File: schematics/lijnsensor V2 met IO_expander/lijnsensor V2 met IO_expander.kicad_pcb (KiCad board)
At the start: 2 copper layers, 137 x 105 mm, 32 parts, among them J2 Conn_01x05_Pin, U1 USBLC6-2SC6, U10 AS7343xDLG, U11 AS7343xDLG, U12 TCA9535RGER, U2 TCA9548ARGER, U3 TLV75718PDBV, U4 AS7343xDLG, U5 AS7343xDLG, U6 AS7343xDLG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

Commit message: begin al met het toevoegen van de io extender nog niet klaar
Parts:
- added H1: MountingHole, MountingHole:MountingHole_4.3mm_M4, F.Cu at (145.0, 70.5)
- added H2: MountingHole, MountingHole:MountingHole_4.3mm_M4, F.Cu at (145.0, 56.5)
- added H3: MountingHole, MountingHole:MountingHole_4.3mm_M4, F.Cu at (90.5, 56.5)
- added H4: MountingHole, MountingHole:MountingHole_4.3mm_M4, F.Cu at (90.5, 70.5)
- added H5: MountingHole, MountingHole:MountingHole_8.4mm_M8, F.Cu at (56.0, 150.0)
- added H6: MountingHole, MountingHole:MountingHole_8.4mm_M8, F.Cu at (181.0, 150.0)
- U12: footprint Package_DFN_QFN:VQFN-24-1EP_4x4mm_P0.5mm_EP2.45x2.45mm -> Package_DFN_QFN:Texas_RGE0024H_VQFN-24-1EP_4x4mm_P0.5mm_EP2.7x2.7mm
- U2: footprint Package_DFN_QFN:Texas_RGE0024C_VQFN-24-1EP_4x4mm_P0.5mm_EP2.1x2.1mm -> Package_DFN_QFN:Texas_RGE0024H_VQFN-24-1EP_4x4mm_P0.5mm_EP2.7x2.7mm
- moved R10 93.5 mm to (133.7, 57.6)
- moved R3 93.5 mm to (181.2, 137.2)
- moved R9 93.5 mm to (136.2, 55.1)
- moved U4 93.5 mm to (181.0, 140.0)
- moved U7 93.5 mm to (136.0, 58.0)
- moved R4 93.5 mm to (178.7, 139.6)
- moved R5 31.8 mm to (181.1, 105.2)
- moved R7 31.8 mm to (161.6, 80.1)
- moved R6 31.0 mm to (178.9, 107.6)
- moved R8 31.0 mm to (160.8, 82.3)
- moved U5 30.8 mm to (181.0, 108.0)
- moved U6 30.8 mm to (163.0, 83.0)
- moved U12 19.9 mm to (123.0, 59.5), turned to 180 degrees
- moved U2 19.4 mm to (113.0, 59.5), turned to 180 degrees
- moved R17 9.21 mm to (113.9, 62.9), turned to 0 degrees
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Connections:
- R10 pad 2: Net-(U2-SC0) -> Net-(U2-SC3)
- R3 pad 2: Net-(U2-SD3) -> Net-(U2-SD0)
- R4 pad 2: Net-(U2-SC3) -> Net-(U2-SC0)
- R5 pad 2: Net-(U2-SD2) -> Net-(U2-SD1)
- R6 pad 2: Net-(U2-SC2) -> Net-(U2-SC1)
- R7 pad 2: Net-(U2-SD1) -> Net-(U2-SC2)
- R8 pad 2: Net-(U2-SC1) -> Net-(U2-SD2)
- R9 pad 2: Net-(U2-SD0) -> Net-(U2-SD3)
- U10 pad 6: unconnected-(U10-GPIO-Pad6) -> Net-(U10-GPIO)
- U10 pad 7: unconnected-(U10-INT-Pad7) -> Net-(U10-INT)
- U11 pad 6: unconnected-(U11-GPIO-Pad6) -> Net-(U11-GPIO)
- U11 pad 7: unconnected-(U11-INT-Pad7) -> Net-(U11-INT)
- U12 pad 1: unconnected-(U12-P00-Pad1) -> Net-(U12-P00)
- U12 pad 10: unconnected-(U12-P10-Pad10) -> Net-(U12-P10)
- U12 pad 11: unconnected-(U12-P11-Pad11) -> Net-(U12-P11)
- U12 pad 12: unconnected-(U12-P12-Pad12) -> Net-(U12-P12)
- U12 pad 13: unconnected-(U12-P13-Pad13) -> Net-(U12-P13)
- U12 pad 14: unconnected-(U12-P14-Pad14) -> Net-(U12-P14)
- U12 pad 15: unconnected-(U12-P15-Pad15) -> Net-(U12-P15)
- U12 pad 16: unconnected-(U12-P16-Pad16) -> Net-(U10-INT)
- U12 pad 17: unconnected-(U12-P17-Pad17) -> Net-(U11-INT)
- U12 pad 2: unconnected-(U12-P01-Pad2) -> Net-(U12-P01)
- U12 pad 3: unconnected-(U12-P02-Pad3) -> Net-(U12-P02)
- U12 pad 4: unconnected-(U12-P03-Pad4) -> Net-(U12-P03)
- U12 pad 5: unconnected-(U12-P04-Pad5) -> Net-(U12-P04)
- U12 pad 6: unconnected-(U12-P05-Pad6) -> Net-(U12-P05)
- U12 pad 7: unconnected-(U12-P06-Pad7) -> Net-(U10-GPIO)
- U12 pad 8: unconnected-(U12-P07-Pad8) -> Net-(U11-GPIO)
- U2 pad 25: unconnected-(U2-1EP-Pad25) -> GND
- U4 pad 2: Net-(U2-SC3) -> Net-(U2-SC0)
- U4 pad 6: unconnected-(U4-GPIO-Pad6) -> Net-(U12-P00)
- U4 pad 7: unconnected-(U4-INT-Pad7) -> Net-(U12-P10)
- U4 pad 8: Net-(U2-SD3) -> Net-(U2-SD0)
- U5 pad 2: Net-(U2-SC2) -> Net-(U2-SC1)
- U5 pad 6: unconnected-(U5-GPIO-Pad6) -> Net-(U12-P01)
- U5 pad 7: unconnected-(U5-INT-Pad7) -> Net-(U12-P11)
- U5 pad 8: Net-(U2-SD2) -> Net-(U2-SD1)
- U6 pad 2: Net-(U2-SC1) -> Net-(U2-SD2)
- U6 pad 6: unconnected-(U6-GPIO-Pad6) -> Net-(U12-P02)
- U6 pad 7: unconnected-(U6-INT-Pad7) -> Net-(U12-P12)
- U6 pad 8: Net-(U2-SD1) -> Net-(U2-SC2)
- U7 pad 2: Net-(U2-SC0) -> Net-(U2-SC3)
- U7 pad 6: unconnected-(U7-GPIO-Pad6) -> Net-(U12-P03)
- U7 pad 7: unconnected-(U7-INT-Pad7) -> Net-(U12-P13)
- U7 pad 8: Net-(U2-SD0) -> Net-(U2-SD3)
- U8 pad 6: unconnected-(U8-GPIO-Pad6) -> Net-(U12-P04)
- U8 pad 7: unconnected-(U8-INT-Pad7) -> Net-(U12-P14)
- U9 pad 6: unconnected-(U9-GPIO-Pad6) -> Net-(U12-P05)
- U9 pad 7: unconnected-(U9-INT-Pad7) -> Net-(U12-P15)
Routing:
- net Net-(U2-SC0): track 118.9 -> 1.98 mm
- net Net-(U2-SD0): track 117.4 -> 2.95 mm, vias 2 -> 1
- net Net-(U2-SD1): track 87.1 -> 1.73 mm, vias 2 -> 0
- net Net-(U2-SC1): track 87.0 -> 1.86 mm, vias 2 -> 0
- net Net-(U11-GPIO): track 0.00 -> 83.1 mm
- net Net-(U11-INT): track 0.00 -> 83.0 mm
- net Net-(U10-GPIO): track 0.00 -> 62.3 mm
- net Net-(U10-INT): track 0.00 -> 55.5 mm
- net Net-(U2-SC2): track 57.9 -> 3.68 mm, vias 2 -> 1
- net Net-(U2-SD2): track 54.9 -> 6.13 mm
- net Net-(U12-P15): track 0.00 -> 33.2 mm, vias 0 -> 1
- net Net-(U12-P05): track 0.00 -> 29.6 mm, vias 0 -> 1
- net Net-(U2-SD3): track 18.7 -> 1.89 mm, vias 2 -> 0
- net Net-(U2-SC3): track 15.7 -> 2.09 mm
- net +3.3V: track 11.3 -> 24.7 mm, vias 3 -> 6
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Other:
- outline, holes or cut-outs redrawn

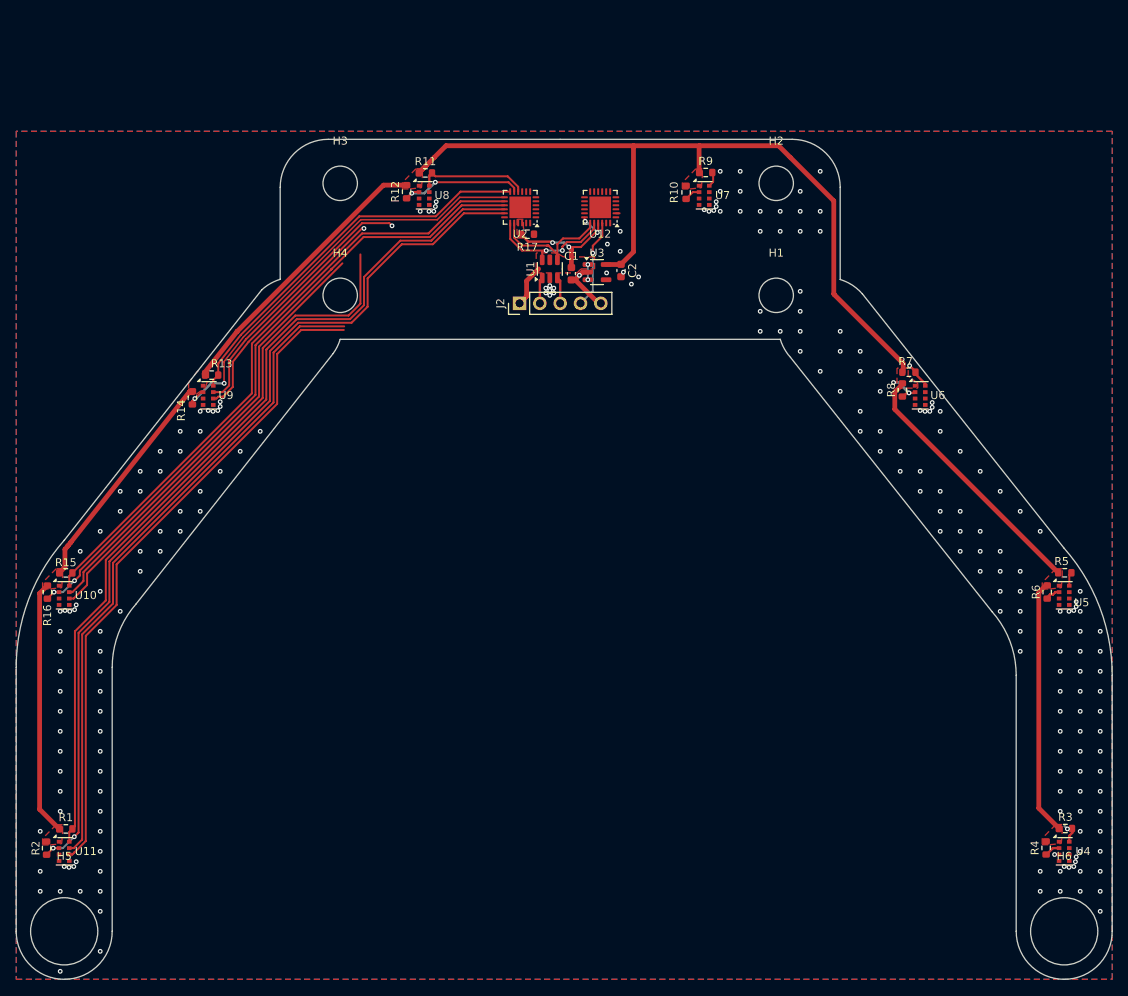
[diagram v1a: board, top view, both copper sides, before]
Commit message: de linker kant is al klaar nu nog de rechter kant van lijnsensor V2 met IO_expander
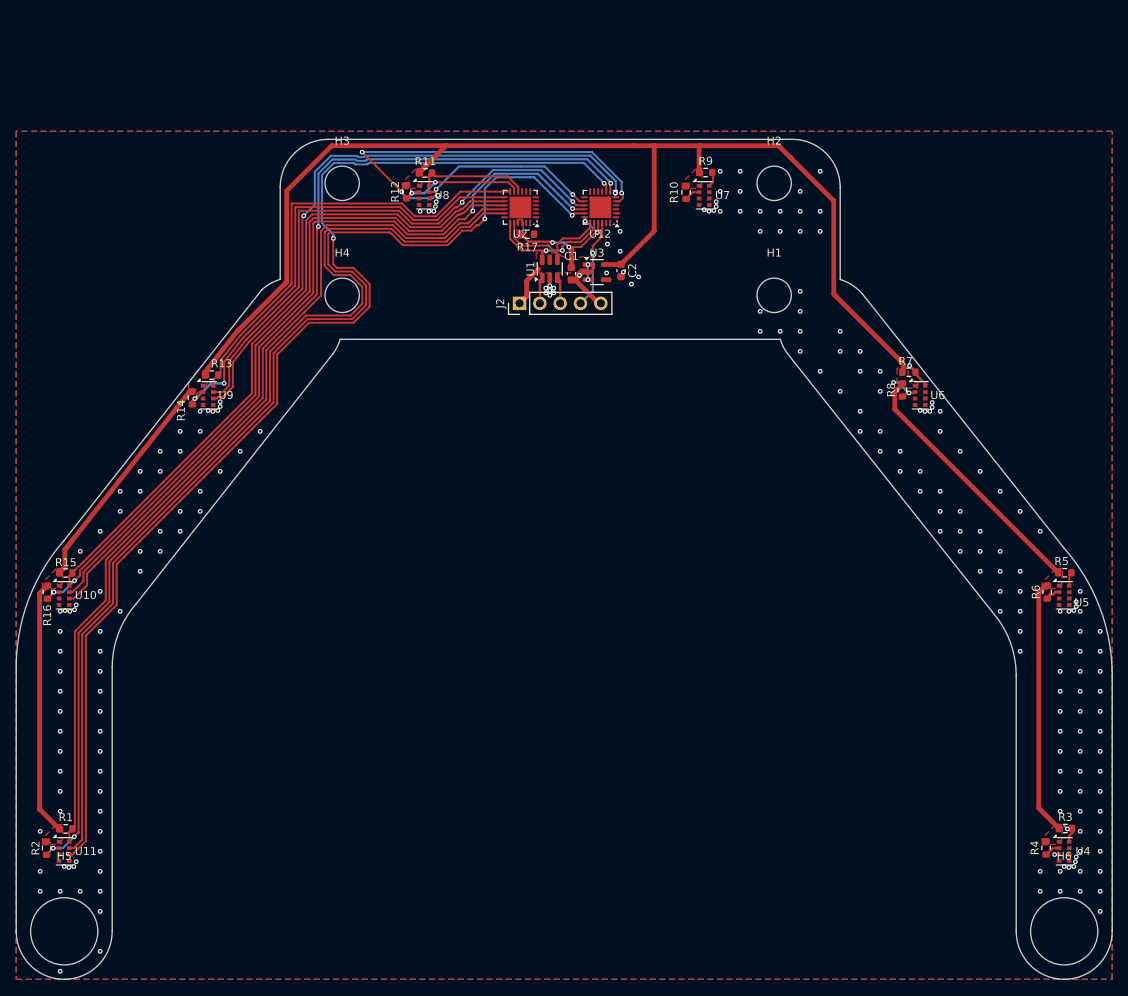
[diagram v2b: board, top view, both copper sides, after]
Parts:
- moved H1 0.25 mm to (144.8, 70.5)
- moved H2 0.25 mm to (144.8, 56.5)
- moved H3 0.25 mm to (90.8, 56.5)
- moved H4 0.25 mm to (90.8, 70.5)
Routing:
- net Net-(U11-GPIO): track 83.1 -> 145.9 mm, vias 0 -> 2
- net Net-(U11-INT): track 83.0 -> 139.5 mm, vias 0 -> 2
- net Net-(U12-P04): track 0.00 -> 50.6 mm, vias 0 -> 4
- net Net-(U12-P05): track 29.6 -> 76.0 mm, vias 1 -> 2
- net Net-(U10-INT): track 55.5 -> 99.7 mm, vias 0 -> 2
- net Net-(U10-GPIO): track 62.3 -> 106.1 mm, vias 0 -> 2
- net Net-(U12-P15): track 33.2 -> 68.7 mm, vias 1 -> 2
- net Net-(U12-P14): track 0.00 -> 22.5 mm, vias 0 -> 2
- net +1V8: track 263.1 -> 277.8 mm
- net Net-(U11-SCL): track 114.5 -> 126.8 mm
- net Net-(U2-SC5): track 53.3 -> 63.0 mm
- net Net-(U2-SD5): track 48.7 -> 55.9 mm
- net Net-(U10-SDA): track 78.7 -> 85.0 mm
- net Net-(U10-SCL): track 82.3 -> 88.5 mm
- net Net-(U11-SDA): track 111.1 -> 115.0 mm

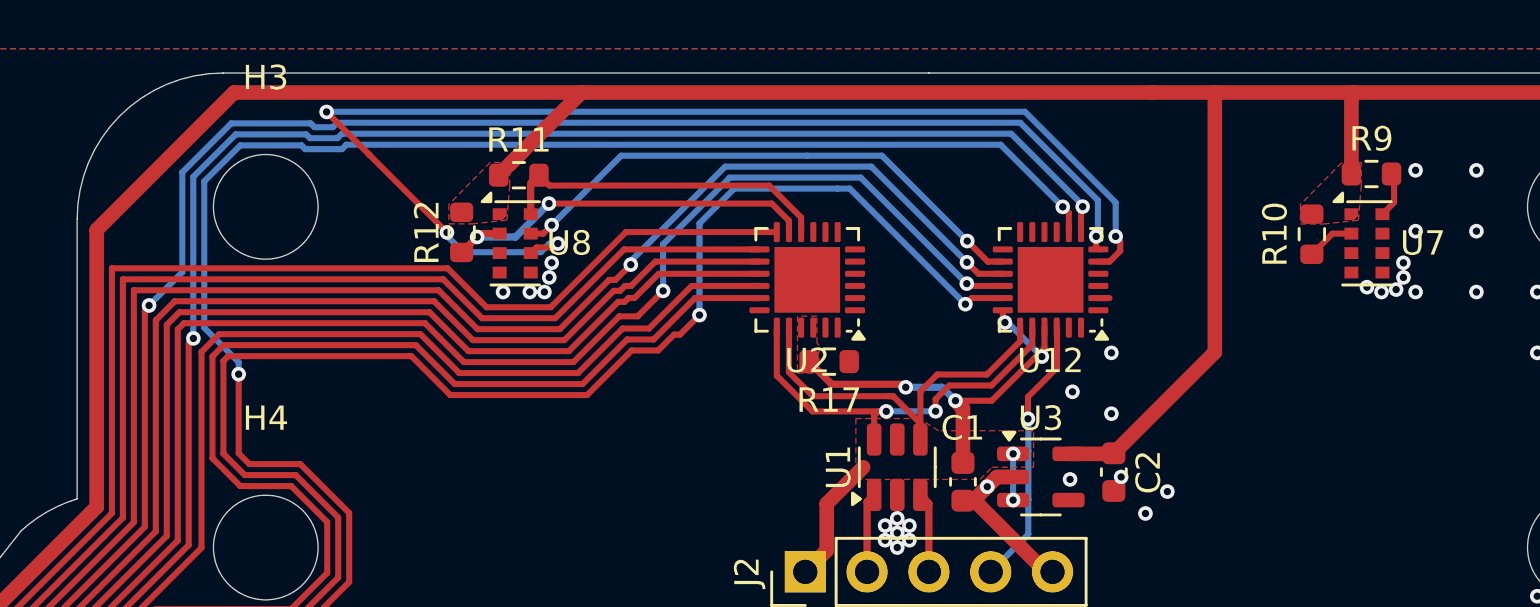
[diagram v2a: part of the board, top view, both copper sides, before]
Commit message: al begonnen aan de rechterkand van lijnsensor V2 met IO_expander
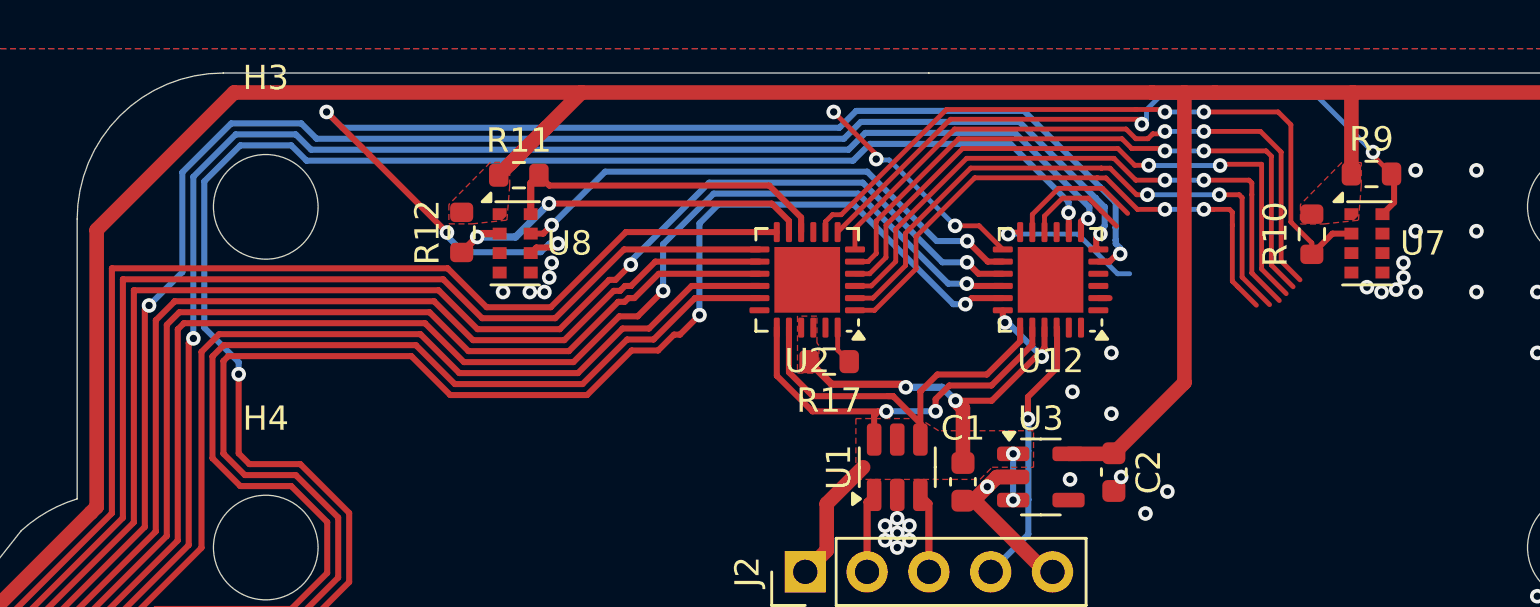
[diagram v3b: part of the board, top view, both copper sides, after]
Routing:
- net Net-(U2-SC3): track 2.09 -> 29.5 mm, vias 0 -> 2
- net Net-(U2-SD3): track 1.89 -> 28.8 mm, vias 0 -> 2
- net Net-(U2-SC2): track 3.68 -> 30.0 mm, vias 1 -> 3
- net Net-(U2-SD2): track 6.13 -> 32.1 mm, vias 2 -> 4
- net Net-(U2-SC1): track 1.86 -> 27.5 mm, vias 0 -> 2
- net Net-(U2-SD1): track 1.73 -> 26.7 mm, vias 0 -> 2
- net Net-(U2-SC0): track 1.98 -> 26.2 mm, vias 0 -> 2
- net Net-(U2-SD0): track 2.95 -> 26.3 mm, vias 1 -> 3
- net Net-(U12-P13): track 0.00 -> 9.40 mm, vias 0 -> 3
- net Net-(U12-P12): track 0.00 -> 6.20 mm, vias 0 -> 1
- net Net-(U12-P11): track 0.00 -> 5.51 mm
- net Net-(U12-P10): track 0.00 -> 4.40 mm
- net Net-(U2-~{RESET}): track 0.00 -> 1.59 mm
- net Net-(U10-GPIO): track 106.1 -> 107.4 mm
- net Net-(U11-GPIO): track 145.9 -> 146.6 mm
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
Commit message: klaar met het tekenen van alle verbindingen en veel via's geplaatst
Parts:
- moved R7 0.29 mm to (161.3, 80.1)
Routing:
- net Net-(U12-P10): track 4.40 -> 120.4 mm, vias 0 -> 4
- net Net-(U12-P00): track 0.00 -> 113.1 mm, vias 0 -> 4
- net Net-(U2-SC0): track 26.2 -> 131.3 mm
- net Net-(U2-SD0): track 26.3 -> 130.5 mm, vias 3 -> 4
- net Net-(U12-P11): track 5.51 -> 92.4 mm, vias 0 -> 4
- net Net-(U12-P01): track 0.46 -> 84.1 mm, vias 0 -> 4
- net Net-(U2-SD1): track 26.7 -> 103.2 mm, vias 2 -> 4
- net Net-(U2-SC1): track 27.5 -> 100.6 mm, vias 2 -> 4
- net Net-(U12-P02): track 0.00 -> 53.4 mm, vias 0 -> 4
- net Net-(U12-P12): track 6.20 -> 56.2 mm, vias 1 -> 4
- net Net-(U2-SC2): track 30.0 -> 68.4 mm, vias 3 -> 4
- net Net-(U2-SD2): track 32.1 -> 70.6 mm
- net Net-(U12-P13): track 9.40 -> 37.9 mm, vias 3 -> 4
- net Net-(U12-P03): track 0.00 -> 14.4 mm, vias 0 -> 2
- net GND: vias 221 -> 1595
